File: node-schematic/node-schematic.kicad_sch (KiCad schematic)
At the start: 0 parts

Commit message: added source information for nrf52840
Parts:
- added U1: NRF52840-QFAA-R7, QFN48_NRF52840-QFAA-R7_NOR, symbol nrf:NRF52840-QFAA-R7
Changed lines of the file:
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@@
 	(generator_version "9.0")
 	(paper "A4")
+	(symbol
+		(lib_id "nrf:NRF52840-QFAA-R7")
+		(at 38.1 35.56 0)
+		(unit 1)
+		(exclude_from_sim no)
+		(in_bom yes)
+		(on_board yes)
+		(dnp no)
+		(fields_autoplaced yes)
+		(property "Reference" "U1"
+			(at 60.96 24.13 0)
+			(effects
+				(font
+					(size 1.8288 1.8288)
+				)
+			)
+		)
+		(property "Value" "NRF52840-QFAA-R7"
+			(at 60.96 27.94 0)
+			(effects
+				(font
+					(size 1.8288 1.8288)
+				)
+			)
+		)
+		(property "Footprint" "QFN48_NRF52840-QFAA-R7_NOR"
+			(at 38.1 35.56 0)
+			(effects
+				(font
+					(size 1.27 1.27)
+				)
+				(hide yes)
+			)
+		)
+		(property "Datasheet" ""
+			(at 38.1 35.56 0)
+			(effects
+				(font
+					(size 1.27 1.27)
+				)
+				(hide yes)
+			)
+		)
+		(property "Description" "Description"
+			(at 38.1 35.56 0)
+			(effects
+				(font
+					(size 1.27 1.27)
+				)
+				(hide yes)
+			)
+		)
+		(property "Copyright" "Copyright (C) 2025 Ultra Librarian. All rights reserved."
+			(at 38.1 35.56 0)
+			(effects
+				(font
+					(size 0.9144 0.9144)
+				)
+				(hide yes)
+			)
+		)
+		(property "Manufacturer_Name" "Nordic Semiconductor"
+			(at 38.1 35.56 0)
+			(effects
+				(font
+					(size 0.9144 0.9144)
+				)
+				(hide yes)
+			)
+		)
+		(property "Manufacturer_Part_Number" "NRF52840-QFAA-R7"
+			(at 38.1 35.56 0)
+			(effects
+				(font
+					(size 0.9144 0.9144)
+				)
+				(hide yes)
+			)
+		)
+		(property "Description_1" "Description"
+			(at 38.1 35.56 0)
+			(effects
+				(font
+					(size 0.9144 0.9144)
+				)
+				(hide yes)
+			)
+		)
+		(property "RefDes" "RefDes"
+			(at 60.96 25.4 0)
+			(effects
+				(font
+					(size 1.4478 1.4478)
+				)
+				(hide yes)
+			)
+		)
+		(property "Type" "Type"
+			(at 60.96 27.94 0)
+			(effects
+				(font
+					(size 1.4478 1.4478)
+				)
+				(hide yes)
+			)
+		)
+		(pin "2"
+		)
+		(pin "1"
+		)
+		(pin "3"
+		)
+		(pin "4"
+		)
+		(pin "5"
+		)
+		(pin "8"
+		)
+		(pin "6"
+		)
+		(pin "17"
+		)
+		(pin "43"
+		)
+		(pin "49"
+		)
+		(pin "40"
+		)
+		(pin "24"
+		)
+		(pin "46"
+		)
+		(pin "36"
+		)
+		(pin "10"
+		)
+		(pin "14"
+		)
+		(pin "20"
+		)
+		(pin "18"
+		)
+		(pin "11"
+		)
+		(pin "22"
+		)
+		(pin "44"
+		)
+		(pin "19"
+		)
+		(pin "21"
+		)
+		(pin "7"
+		)
+		(pin "15"
+		)
+		(pin "13"
+		)
+		(pin "23"
+		)
+		(pin "48"
+		)
+		(pin "16"
+		)
+		(pin "47"
+		)
+		(pin "9"
+		)
+		(pin "12"
+		)
+		(pin "45"
+		)
+		(pin "42"
+		)
+		(pin "41"
+		)
+		(pin "39"
+		)
+		(pin "38"
+		)
+		(pin "37"
+		)
+		(pin "28"
+		)
+		(pin "32"
+		)
+		(pin "30"
+		)
+		(pin "31"
+		)
+		(pin "26"
+		)
+		(pin "27"
+		)
+		(pin "34"
+		)
+		(pin "33"
+		)
+		(pin "25"
+		)
+		(pin "35"
+		)
+		(pin "29"
+		)
+		(instances
+			(project ""
+				(path "/92f6ad1b-5cba-44e2-b81f-560b2afef862"
+					(reference "U1")
+					(unit 1)
+				)
+			)
+		)
+	)
 	(sheet_instances
 		(path "/"

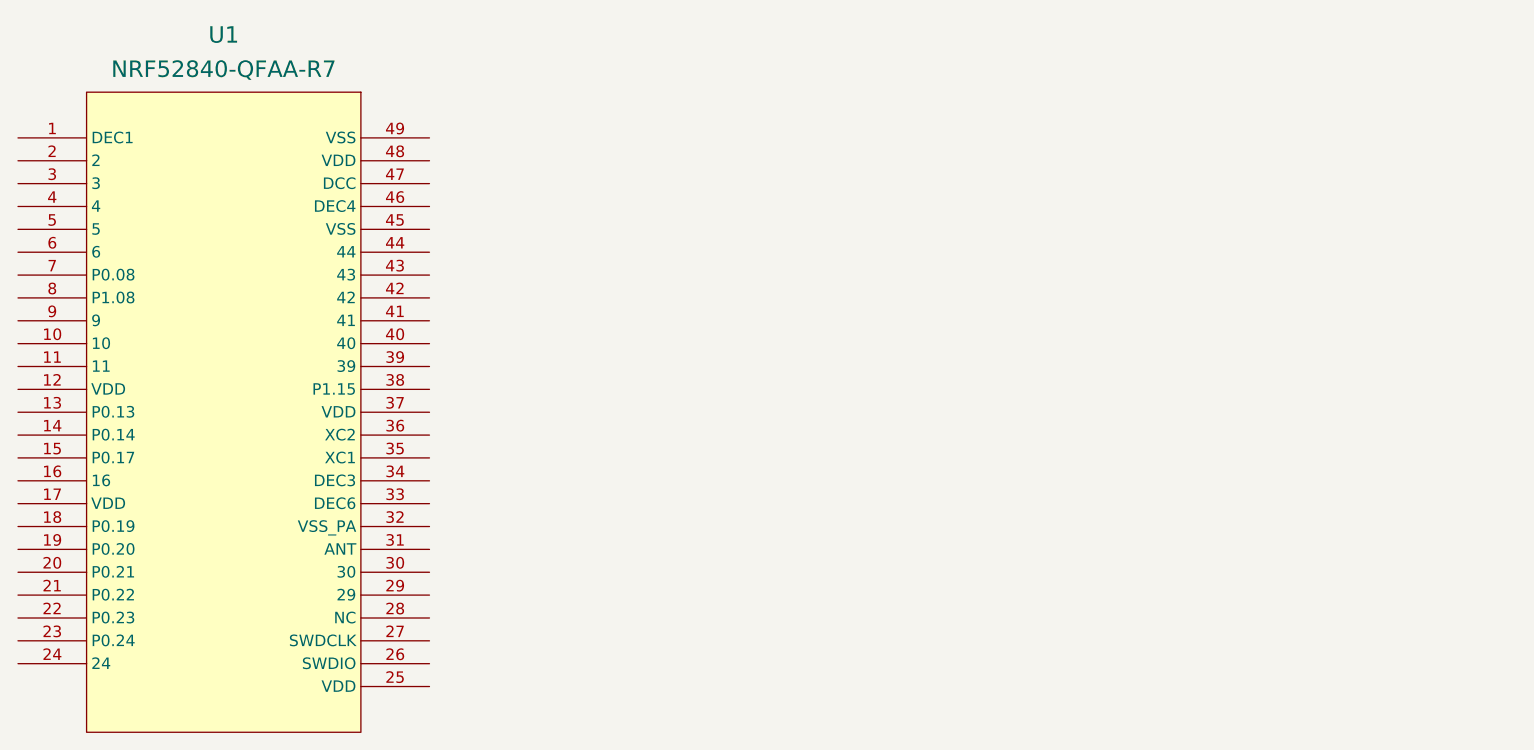
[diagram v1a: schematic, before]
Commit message: updated NRF schematic labels
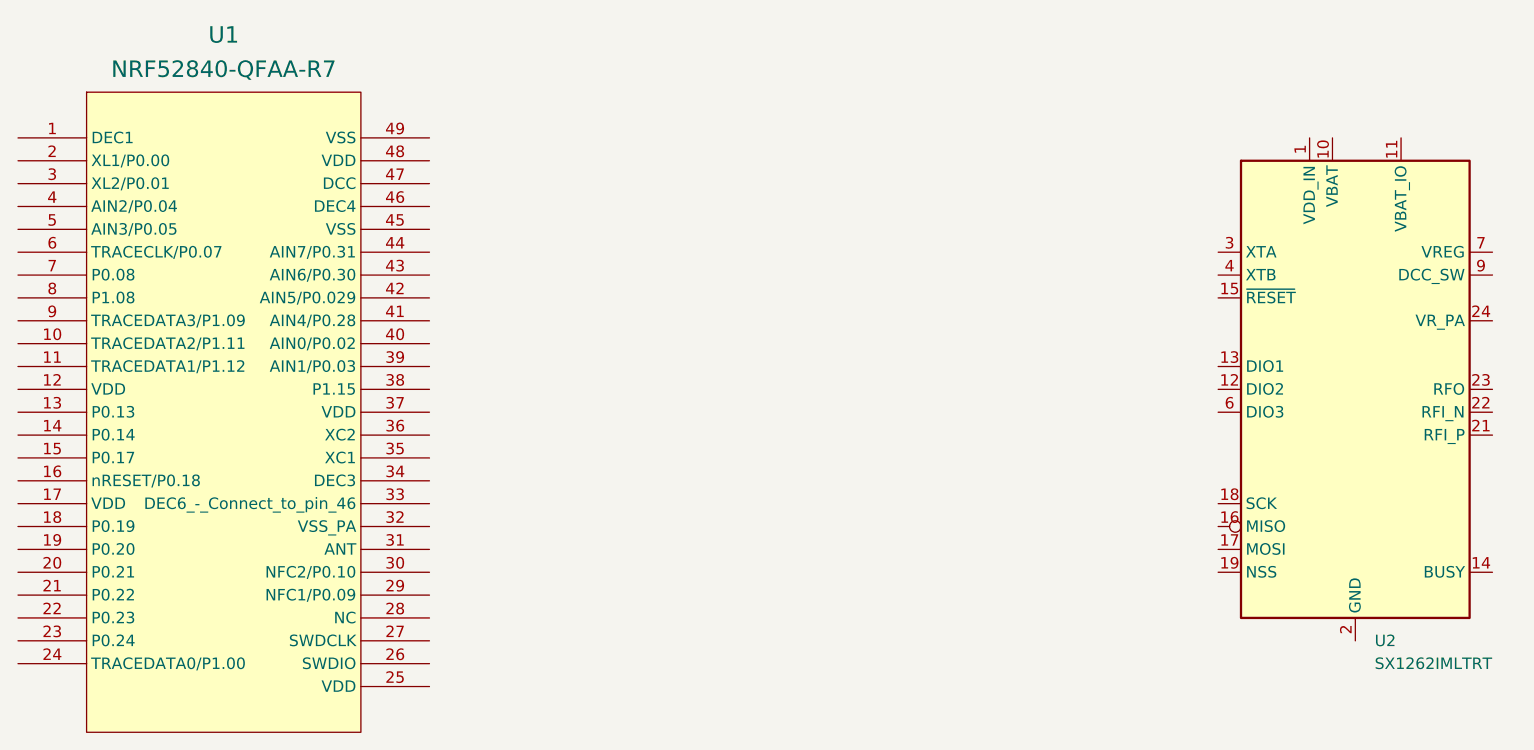
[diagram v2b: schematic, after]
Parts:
- added U2: SX1262IMLTRT, Package_DFN_QFN:QFN-24-1EP_4x4mm_P0.5mm_EP2.6x2.6mm, symbol RF:SX1262IMLTRT
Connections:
- new net: U2.2 (GND), U2.20 (GND), U2.25 (GND), U2.5 (GND), U2.8 (GND)
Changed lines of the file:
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@@
 	(paper "A4")
+	(symbol
+		(lib_id "RF:SX1262IMLTRT")
+		(at 186.69 63.5 0)
+		(unit 1)
+		(exclude_from_sim no)
+		(in_bom yes)
+		(on_board yes)
+		(dnp no)
+		(fields_autoplaced yes)
+		(property "Reference" "U2"
+			(at 188.8333 91.44 0)
+			(effects
+				(font
+					(size 1.27 1.27)
+				)
+				(justify left)
+			)
+		)
+		(property "Value" "SX1262IMLTRT"
+			(at 188.8333 93.98 0)
+			(effects
+				(font
+					(size 1.27 1.27)
+				)
+				(justify left)
+			)
+		)
+		(property "Footprint" "Package_DFN_QFN:QFN-24-1EP_4x4mm_P0.5mm_EP2.6x2.6mm"
+			(at 187.96 95.25 0)
+			(effects
+				(font
+					(size 1.27 1.27)
+				)
+				(hide yes)
+			)
+		)
+		(property "Datasheet" "https://semtech.file.force.com/sfc/dist/version/download/?oid=00DE0000000JelG&ids=0682R00000IjPWSQA3&d=%2Fa%2F2R000000Un7F%2FyT.fKdAr9ZAo3cJLc4F2cBdUsMftpT2vsOICP7NmvMo"
+			(at 187.96 92.71 0)
+			(effects
+				(font
+					(size 1.27 1.27)
+				)
+				(hide yes)
+			)
+		)
+		(property "Description" "150 MHz to 960 MHz Low Power Long Range Transceiver, 22dBm output power, spreading factor from 5 to 12, LoRA, QFN-24"
+			(at 186.69 63.5 0)
+			(effects
+				(font
+					(size 1.27 1.27)
+				)
+				(hide yes)
+			)
+		)
+		(pin "4"
+		)
+		(pin "9"
+		)
+		(pin "5"
+		)
+		(pin "17"
+		)
+		(pin "21"
+		)
+		(pin "10"
+		)
+		(pin "20"
+		)
+		(pin "15"
+		)
+		(pin "12"
+		)
+		(pin "18"
+		)
+		(pin "13"
+		)
+		(pin "8"
+		)
+		(pin "3"
+		)
+		(pin "16"
+		)
+		(pin "19"
+		)
+		(pin "1"
+		)
+		(pin "6"
+		)
+		(pin "2"
+		)
+		(pin "25"
+		)
+		(pin "11"
+		)
+		(pin "7"
+		)
+		(pin "24"
+		)
+		(pin "23"
+		)
+		(pin "22"
+		)
+		(pin "14"
+		)
+		(instances
+			(project ""
+				(path "/92f6ad1b-5cba-44e2-b81f-560b2afef862"
+					(reference "U2")
+					(unit 1)
+				)
+			)
+		)
+	)
 	(symbol
 		(lib_id "nrf:NRF52840-QFAA-R7")

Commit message: x2 oscilator done
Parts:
- removed U2: SX1262IMLTRT, Package_DFN_QFN:QFN-24-1EP_4x4mm_P0.5mm_EP2.6x2.6mm, symbol RF:SX1262IMLTRT
- added C1: 100nF, symbol Device:C_Small_US
- added C2, C3: 12pF, symbol Device:C_Small_US
- added X2: 32.768kHz, CM8V-T1A-32.768KHZ-9PF-20PPM-TA-QC:XTAL_CM8V-T1A-32.768KHZ-9PF-20PPM-TA-QC, symbol CM8V-T1A-32.768KHZ-9PF-20PPM-TA-QC:CM8V-T1A-32.768KHZ-9PF-20PPM-TA-QC
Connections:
- net at U1.1 (DEC1): now also C1.1
- net at U1.2 (XL1/P0.00): now also C3.2, X2.2
- net at U1.3 (XL2/P0.01): now also C2.2, X2.1
- new net GND: C1.2, C2.1, C3.1
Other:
- moved on the sheet: U1

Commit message: nrf schematic done
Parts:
- added C10: N.C., symbol Device:C_Small_US
- added C11: 100pF, symbol Device:C_Small_US
- added C12, C13: 12pF, symbol Device:C_Small_US
- added C14, C15, C4, C5, C6: 100nF, symbol Device:C_Small_US
- added C16: 1.0uF, symbol Device:C_Small_US
- added C17: 47nF, symbol Device:C_Small_US
- added C7: 1.0pF, symbol Device:C_Small_US
- added C8, C9: 1.2pF, symbol Device:C_Small_US
- added L1, L2: 4.7nH, symbol Device:L
- added L3: 10uH, symbol Device:L
- added L4: 15nH, symbol Device:L
- added X1: NX2016SA-32MHZ, NX2016SA_NDK, symbol 2025-11-05_03-34-29:NX2016SA-32MHZ-EXS00A-CS11336
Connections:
- net GND: now also U1.32 (VSS_PA), U1.33 (DEC6), U1.36 (XC2), U1.49 (VSS), C10.1, C10.2, C11.2, C12.1, C12.2, C13.2, C14.2, C15.2, C16.2, C17.2, C4.2, C5.2, C6.2, C7.2, C8.2, C9.2, X1.1, X1.2, X1.4
- net VDD_nRF: now reaches U1.12 (VDD)
- net VDD_nRF: now also U1.17 (VDD), U1.25 (VDD), U1.37 (VDD), U1.48 (VDD), C14.1, C15.1, C4.1, C5.1, C6.1
- net SWDIO: now reaches U1.26 (SWDIO)
- net SWDCLK: now reaches U1.27 (SWDCLK)
- net at U1.31 (ANT): now also C7.1, L1.1
- net at U1.34 (DEC3): now also C11.1
- net at U1.35 (XC1): now also C13.1, X1.3
- net at U1.46 (DEC4): now also C16.1, C17.1, L4.2
- net at U1.47 (DCC): now also L3.1
- new net: C8.1, L1.2, L2.1
- new net: L3.2, L4.1
- new net RF: C9.1, L2.2
- no-connect marks 0 -> 1

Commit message: pcb layout, no connections
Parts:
- removed C9: 1.2pF, symbol Device:C_Small_US
- removed U1: NRF52840-QFAA-R7, QFN48_NRF52840-QFAA-R7_NOR, symbol nrf:NRF52840-QFAA-R7
- added U1: NRF52840-QFAA-R7, QFN48_NRF52840-QFAA-R7_NOR, symbol 2025-11-05_15-15-41:NRF52840-QFAA-R7
- C1, C10, C11, C12, C13, C14, C17, C2, C3, C4, C5, C6, C7, C8: footprint (none) -> Capacitor_SMD:C_0201_0603Metric
- C15: value 100nF -> 1.0uF; footprint (none) -> Capacitor_SMD:C_0402_1005Metric
- C16, L4: footprint (none) -> Capacitor_SMD:C_0402_1005Metric
- L1, L2: footprint (none) -> Inductor_SMD:L_0201_0603Metric
- L3: footprint (none) -> Capacitor_SMD:C_0603_1608Metric
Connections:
- net GND: now also U1.32 (VSS_PA), U1.33 (DEC6), U1.49 (VSS); no longer C12.1, X1.1
- net SWDCLK: now also U1.27 (SWDCLK)
- net SWDIO: now also U1.26 (SWDIO)
- net VDD_nRF: now also U1.12 (VDD), U1.17 (VDD), U1.25 (VDD), U1.37 (VDD), U1.48 (VDD)
- net at C16.1, C17.1, L4.2: now also U1.46 (DEC4)
- net at C3.2, X2.2: now also U1.2
- net at C7.1, L1.1: now also U1.31 (ANT)
- net at C1.1: now also U1.1 (DEC1)
- net at C11.1: now also U1.34 (DEC3)
- net at C2.2, X2.1: now also U1.3
- net at C13.1, X1.3: now also U1.35 (XC1)
- net at L3.1: now also U1.47 (DCC)
- new net: C12.1, U1.36 (XC2), X1.1

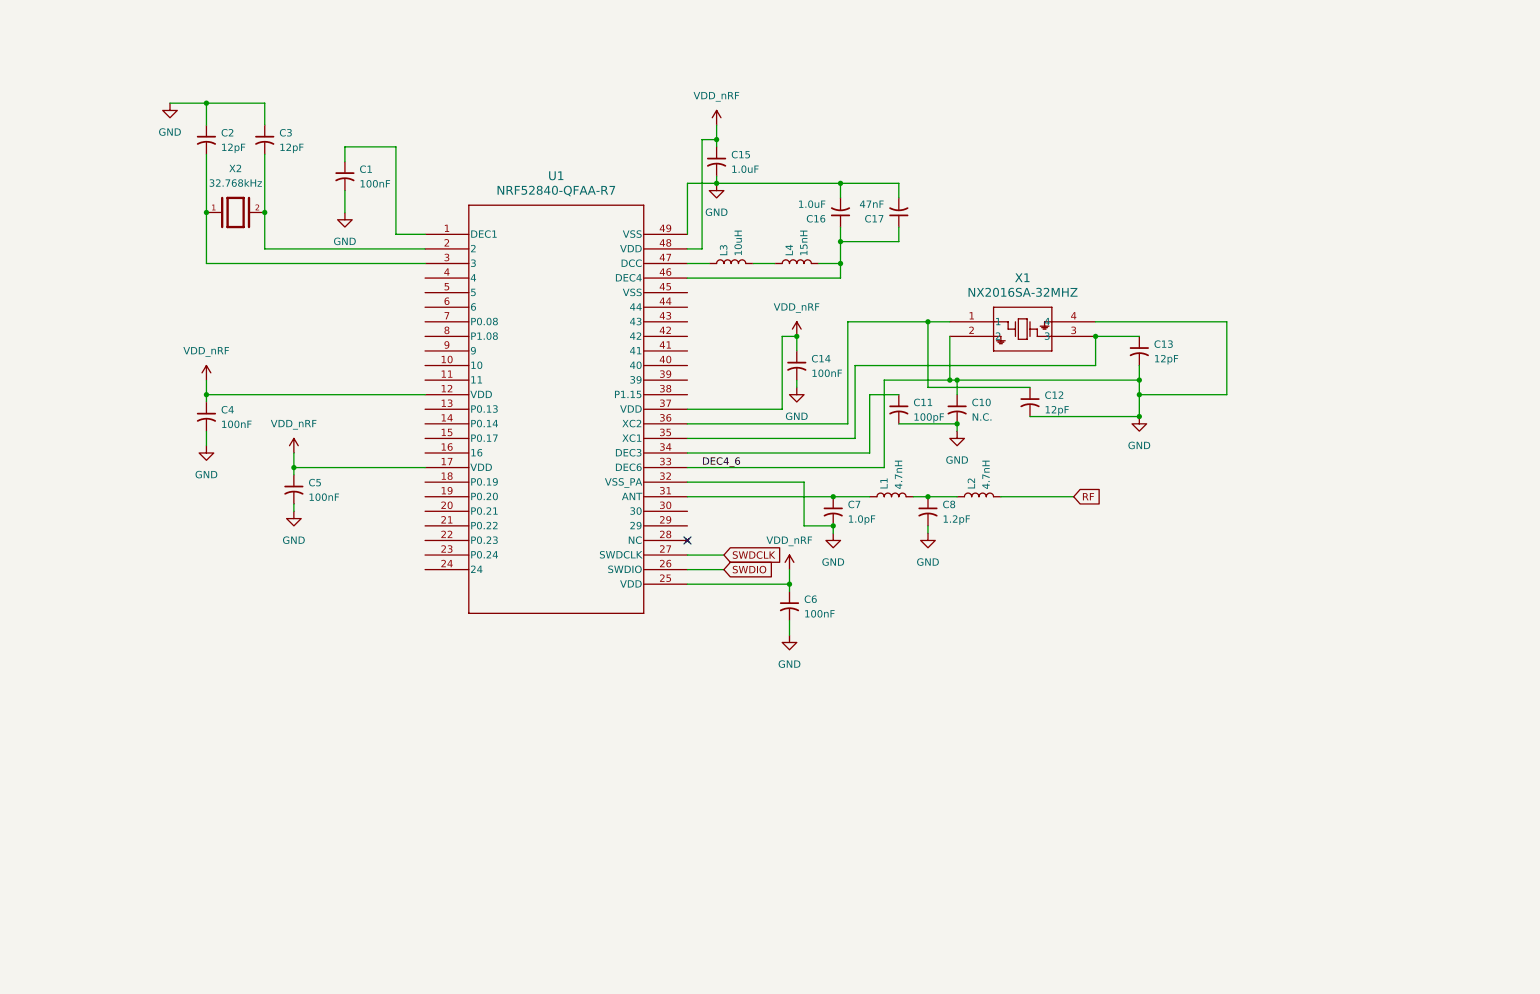
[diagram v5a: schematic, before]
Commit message: added sx1262 sub page
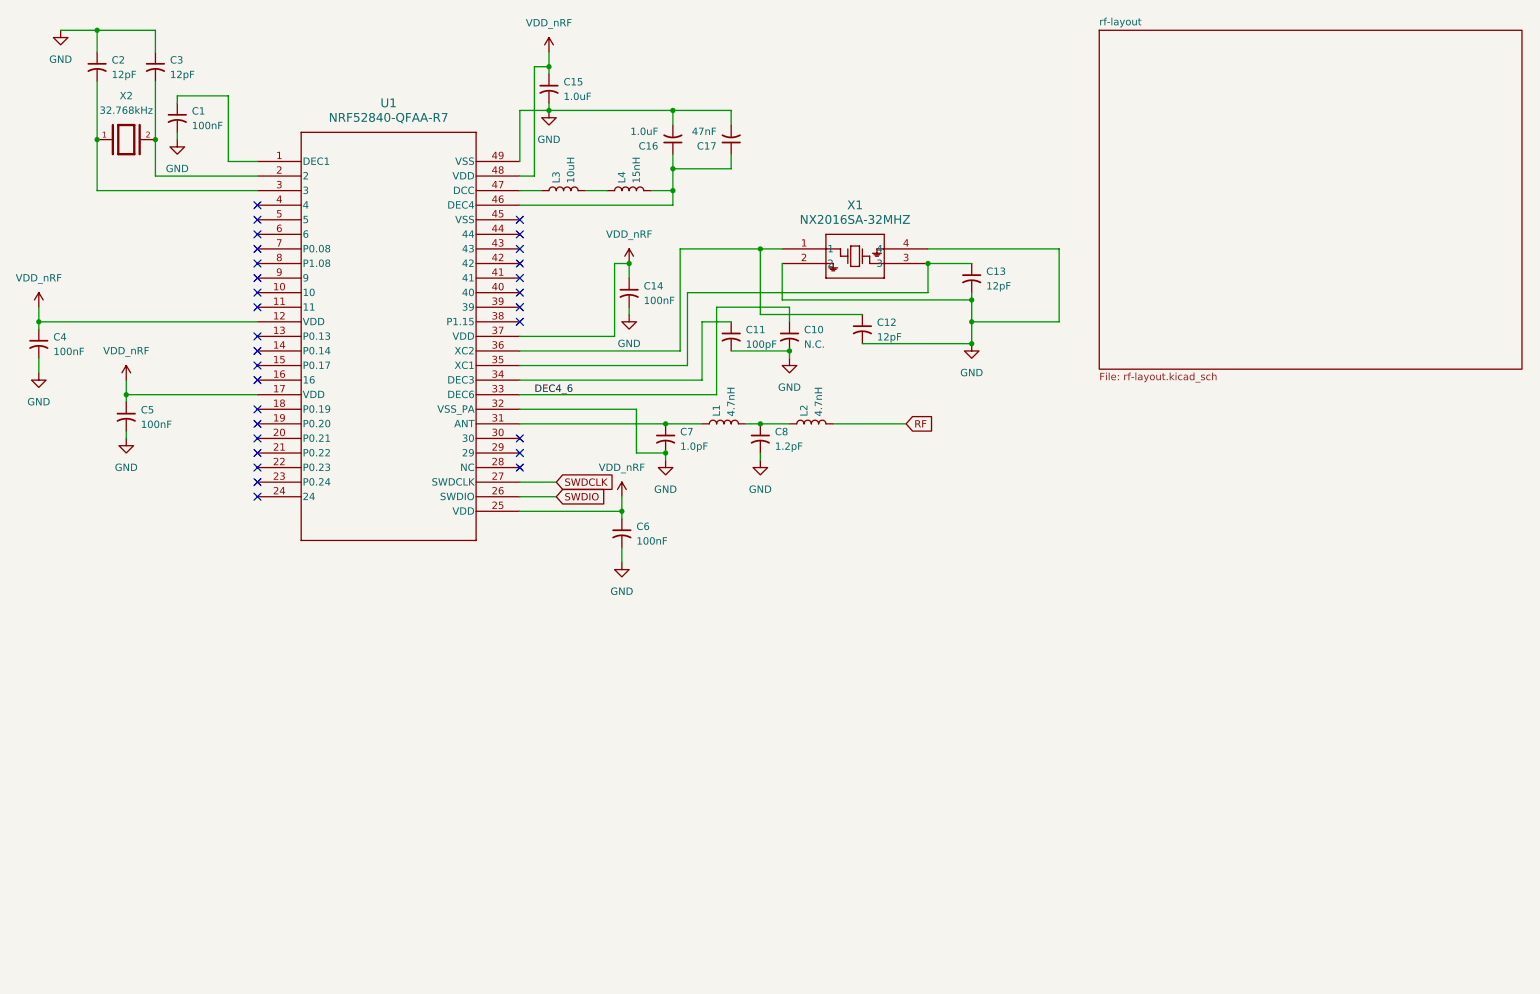
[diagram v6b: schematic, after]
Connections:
- net GND: no longer C10.1, U1.33 (DEC6)
- new net DEC4_6: C10.1, U1.33 (DEC6)
- no-connect marks 1 -> 30
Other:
- added sheet rf-layout (rf-layout.kicad_sch)
- moved on the sheet: C1, C10, C11, C12, C13, C14, C15, C16, C17, C2, C3, C4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
